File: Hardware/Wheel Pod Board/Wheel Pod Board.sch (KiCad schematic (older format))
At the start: 30 parts, among them U1 STM32F401RCT6

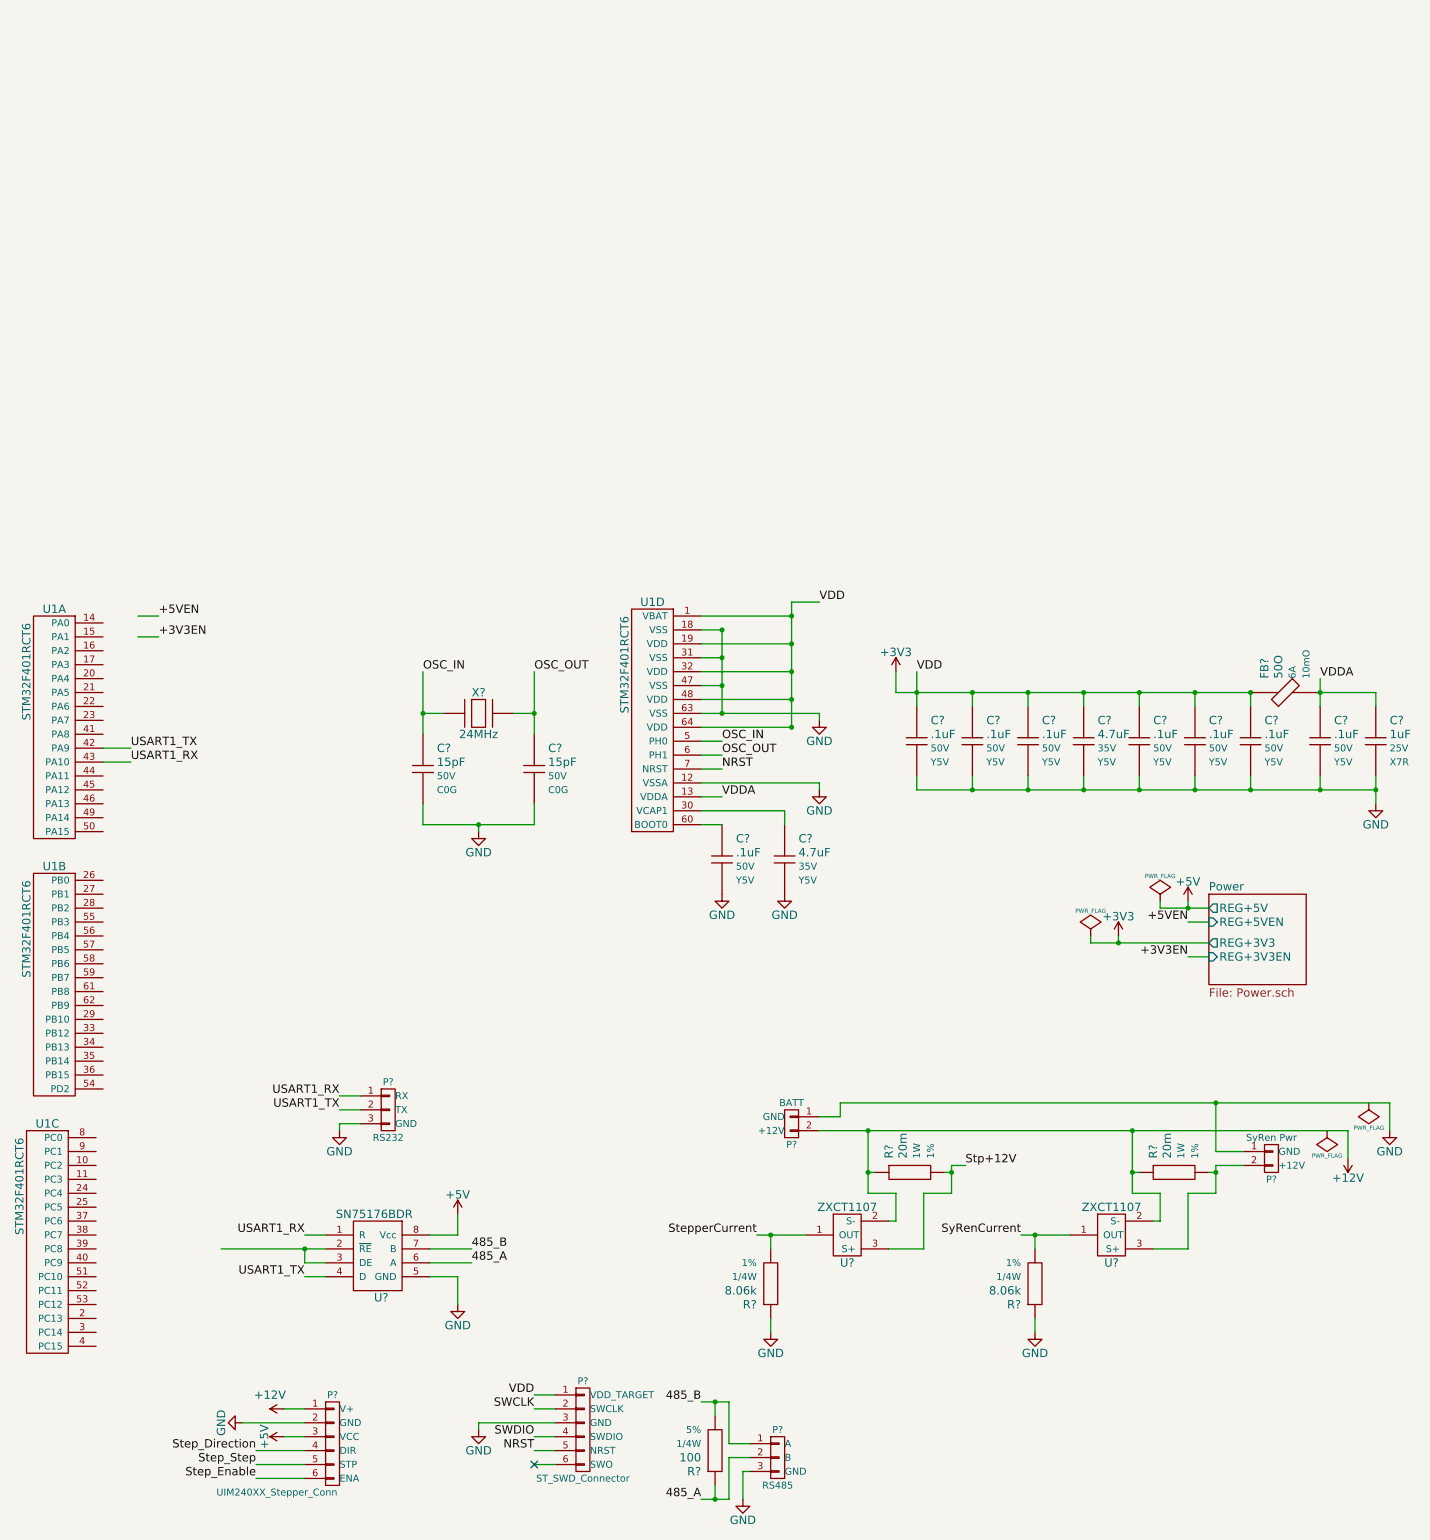
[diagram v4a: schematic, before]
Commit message: Calculate current sense, parts on PCB
Resolves #6
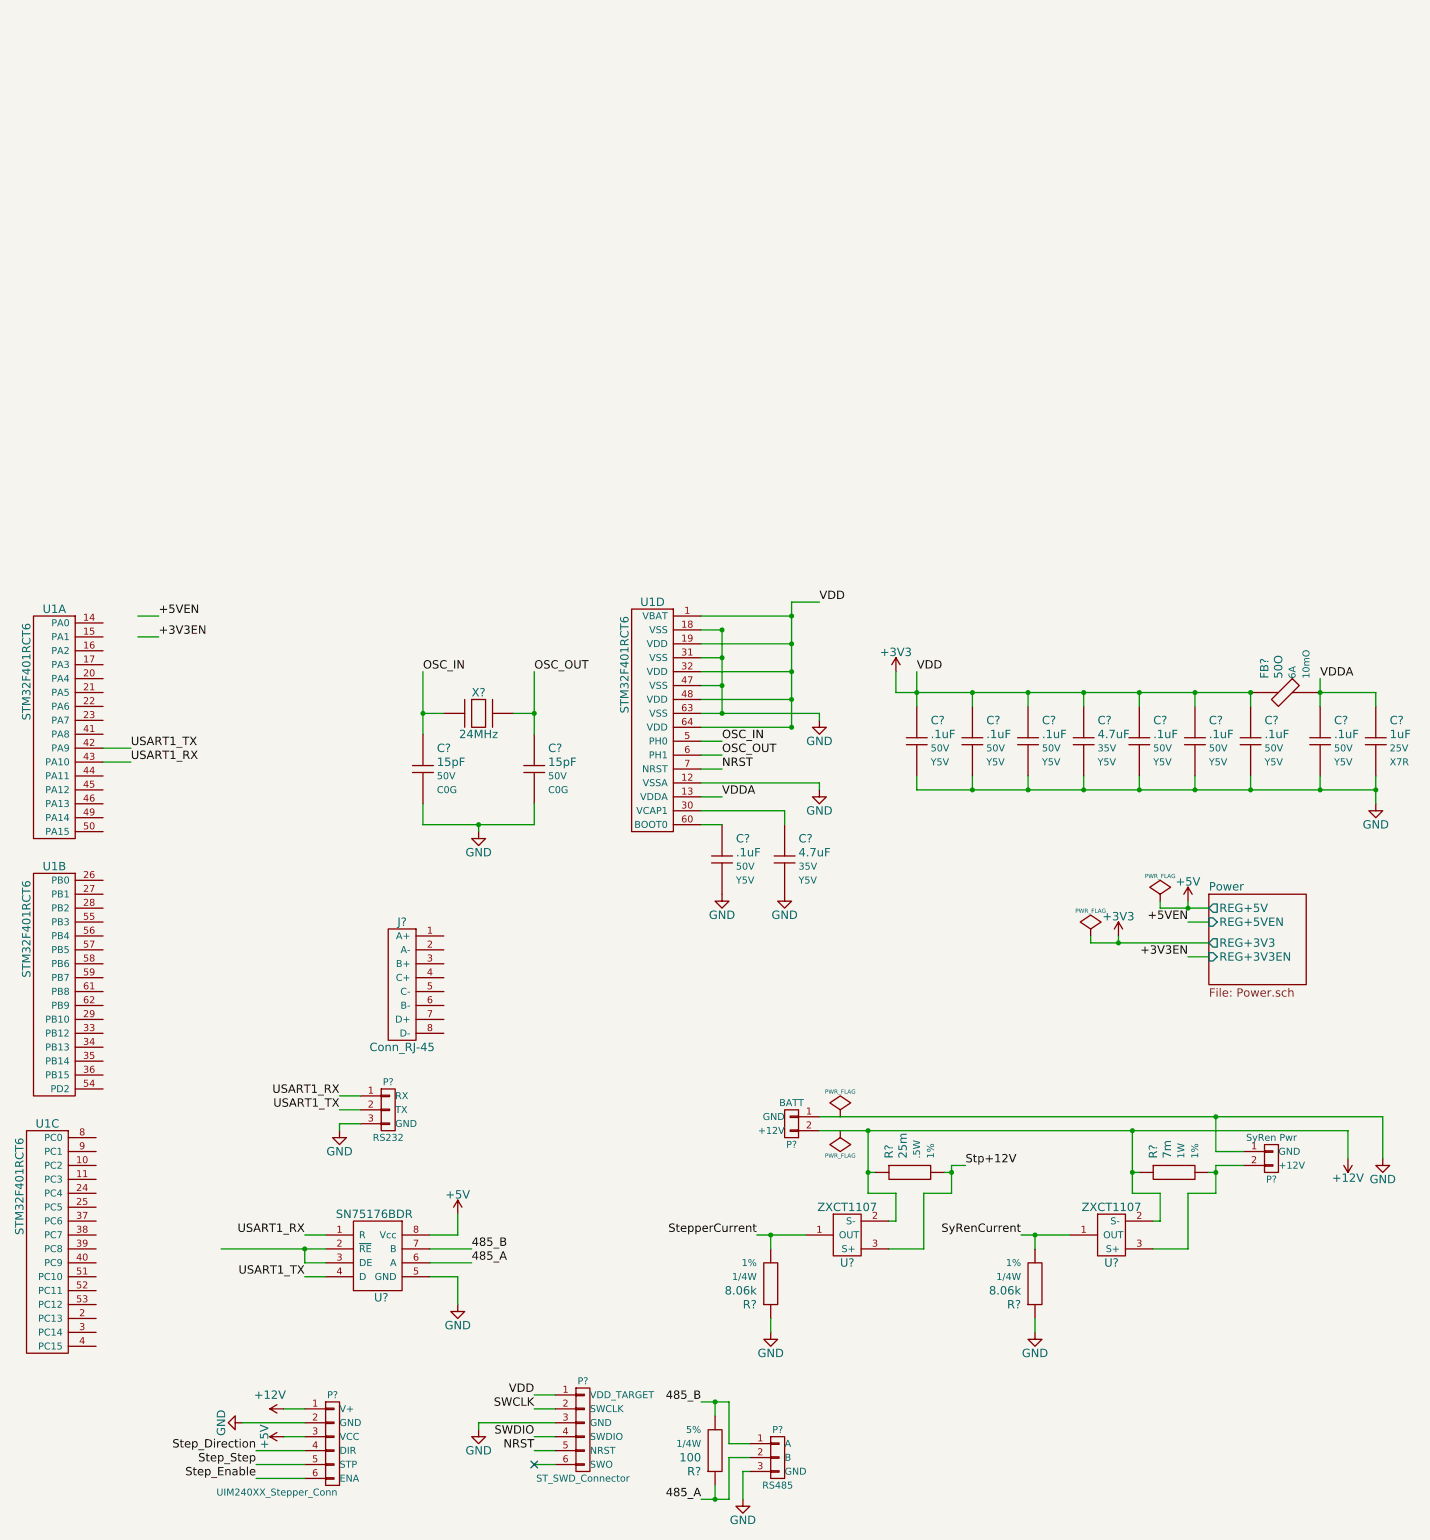
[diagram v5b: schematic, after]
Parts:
- added J?: Conn_RJ-45, symbol Conn_RJ-45
- R?: value 20m -> 25m; Manufacturer Part # LRMAM1206-R02FT5 -> LRC-LRF1206LF-01-R025F; Power 1W -> .5W; Vendor Part # 985-1548-1-ND -> 989-1025-1-ND
- R?: value 20m -> 7m; Manufacturer TT Electronics -> Riedon; Manufacturer Part # LRMAM1206-R02FT5 -> CSR1206-0R007F1; Vendor Part # 985-1548-1-ND -> 696-1373-1-ND
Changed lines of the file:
@@
 LIBS:Passives
 LIBS:MAVRIClib
+LIBS:Connectors
 LIBS:Wheel Pod Board-cache
 EELAYER 25 0
@@
 Connection ~ 6100 1400
 Wire Wire Line
-	5950 1800 6800 1800
+	5950 1800 6100 1800
+Wire Wire Line
+	6100 1800 6800 1800
 Connection ~ 6100 1800
 Wire Wire Line
@@
 Connection ~ 6600 1100
 Wire Wire Line
-	6100 1200 6100 1800
-Wire Wire Line
-	6600 1000 6600 1900
+	6100 1200 6100 1400
+Wire Wire Line
+	6100 1400 6100 1600
+Wire Wire Line
+	6100 1600 6100 1800
+Wire Wire Line
+	6600 1000 6600 1100
+Wire Wire Line
+	6600 1100 6600 1300
+Wire Wire Line
+	6600 1300 6600 1500
+Wire Wire Line
+	6600 1500 6600 1700
+Wire Wire Line
+	6600 1700 6600 1900
 Wire Wire Line
 	5950 2600 6100 2600
@@
 	3100 5750 3250 5750
 Wire Wire Line
-	2500 5650 3250 5650
+	2500 5650 3100 5650
+Wire Wire Line
+	3100 5650 3250 5650
 Wire Wire Line
 	3250 5850 3100 5850
@@
 	9900 1650 9900 1750
 Wire Wire Line
-	7500 1500 7500 1750
+	7500 1500 7500 1650
+Wire Wire Line
+	7500 1650 7500 1750
 Connection ~ 7500 1650
 Wire Wire Line
@@
 Connection ~ 9900 2350
 Wire Wire Line
-	10400 1550 10400 1750
+	10400 1550 10400 1650
+Wire Wire Line
+	10400 1650 10400 1750
 Connection ~ 9900 1650
 Connection ~ 10400 1650
@@
 	10800 1650 10800 1750
 Wire Wire Line
-	10800 2250 10800 2450
+	10800 2250 10800 2350
+Wire Wire Line
+	10800 2350 10800 2450
 Wire Wire Line
 	10400 2350 10400 2250
@@
 	10400 1650 10800 1650
 Wire Wire Line
-	7500 2350 10800 2350
-Wire Wire Line
-	7350 1650 9900 1650
+	7500 2350 7900 2350
+Wire Wire Line
+	7900 2350 8300 2350
+Wire Wire Line
+	8300 2350 8700 2350
+Wire Wire Line
+	8700 2350 9100 2350
+Wire Wire Line
+	9100 2350 9500 2350
+Wire Wire Line
+	9500 2350 9900 2350
+Wire Wire Line
+	9900 2350 10400 2350
+Wire Wire Line
+	10400 2350 10800 2350
+Wire Wire Line
+	7350 1650 7500 1650
+Wire Wire Line
+	7500 1650 7900 1650
+Wire Wire Line
+	7900 1650 8300 1650
+Wire Wire Line
+	8300 1650 8700 1650
+Wire Wire Line
+	8700 1650 9100 1650
+Wire Wire Line
+	9100 1650 9500 1650
+Wire Wire Line
+	9500 1650 9900 1650
 Wire Wire Line
 	7350 1500 7350 1650
@@
 	6150 7150 6150 7450
 Wire Wire Line
-	6150 7450 5950 7450
-Wire Wire Line
-	5950 6750 6150 6750
+	6150 7450 6050 7450
+Wire Wire Line
+	6050 7450 5950 7450
+Wire Wire Line
+	5950 6750 6050 6750
+Wire Wire Line
+	6050 6750 6150 6750
 Wire Wire Line
 	6150 6750 6150 7050
@@
 OSC_OUT
 Wire Wire Line
-	3950 1500 3950 1950
+	3950 1500 3950 1800
+Wire Wire Line
+	3950 1800 3950 1950
 Wire Wire Line
 	3950 1800 4100 1800
@@
 	4600 1800 4750 1800
 Wire Wire Line
-	4750 1500 4750 1950
+	4750 1500 4750 1800
+Wire Wire Line
+	4750 1800 4750 1950
 Wire Wire Line
 	3950 2450 3950 2600
 Wire Wire Line
-	3950 2600 4750 2600
+	3950 2600 4350 2600
+Wire Wire Line
+	4350 2600 4750 2600
 Wire Wire Line
 	4750 2600 4750 2450
@@
 P 7450 5100
 F 0 "R?" V 7300 5200 60  0000 L CNN
-F 1 "20m" V 7400 5200 60  0000 L CNN
+F 1 "25m" V 7400 5200 60  0000 L CNN
 F 2 "Resistors_SMD:R_1206_HandSoldering" H 7350 5100 60  0001 C CNN
 F 3 "" H 7450 5200 60  0001 C CNN
 F 4 "TT Electronics" H 7450 5100 60  0001 C CNN "Manufacturer"
-F 5 "LRMAM1206-R02FT5" H 7450 5100 60  0001 C CNN "Manufacturer Part #"
+F 5 "LRC-LRF1206LF-01-R025F" H 7450 5100 60  0001 C CNN "Manufacturer Part #"
 F 6 "Digi-Key" H 7450 5100 60  0001 C CNN "Vendor"
-F 7 "985-1548-1-ND" H 7450 5100 60  0001 C CNN "Vendor Part #"
-F 8 "1W" V 7500 5200 50  0000 L CNN "Power"
+F 7 "989-1025-1-ND" H 7450 5100 60  0001 C CNN "Vendor Part #"
+F 8 ".5W" V 7500 5200 50  0000 L CNN "Power"
 F 9 "1%" V 7600 5200 50  0000 L CNN "Tolerance"
 	1    7450 5100
@@
 	7350 5250 7350 5450
 Wire Wire Line
-	6350 5550 6700 5550
+	6350 5550 6450 5550
+Wire Wire Line
+	6450 5550 6700 5550
 Wire Wire Line
 	6450 5650 6450 5550
@@
 	7750 5100 7700 5100
 Wire Wire Line
-	7150 4800 7150 5250
+	7150 4800 7150 5100
+Wire Wire Line
+	7150 5100 7150 5250
 Wire Wire Line
 	7200 5100 7150 5100
@@
 $EndComp
 Wire Wire Line
-	8750 3450 9600 3450
+	8750 3450 8950 3450
+Wire Wire Line
+	8950 3450 9600 3450
 Wire Wire Line
 	8950 3450 8950 3400
@@
 $EndComp
 Wire Wire Line
-	9250 3200 9600 3200
+	9250 3200 9450 3200
+Wire Wire Line
+	9450 3200 9600 3200
 Wire Wire Line
 	9250 3200 9250 3150
@@
 $EndComp
 Wire Wire Line
-	7750 5050 7750 5250
+	7750 5050 7750 5100
+Wire Wire Line
+	7750 5100 7750 5250
 Wire Wire Line
 	6450 6150 6450 6250
@@
 StepperCurrent
 Wire Wire Line
-	6800 4800 10600 4800
+	6800 4800 7150 4800
+Wire Wire Line
+	7150 4800 9050 4800
+Wire Wire Line
+	9050 4800 10600 4800
 $Comp
 L ZXCT1107 U?
@@
 P 9350 5100
 F 0 "R?" V 9200 5200 60  0000 L CNN
-F 1 "20m" V 9300 5200 60  0000 L CNN
+F 1 "7m" V 9300 5200 60  0000 L CNN
 F 2 "Resistors_SMD:R_1206_HandSoldering" H 9250 5100 60  0001 C CNN
 F 3 "" H 9350 5200 60  0001 C CNN
-F 4 "TT Electronics" H 9350 5100 60  0001 C CNN "Manufacturer"
-F 5 "LRMAM1206-R02FT5" H 9350 5100 60  0001 C CNN "Manufacturer Part #"
+F 4 "Riedon" H 9350 5100 60  0001 C CNN "Manufacturer"
+F 5 "CSR1206-0R007F1" H 9350 5100 60  0001 C CNN "Manufacturer Part #"
 F 6 "Digi-Key" H 9350 5100 60  0001 C CNN "Vendor"
-F 7 "985-1548-1-ND" H 9350 5100 60  0001 C CNN "Vendor Part #"
+F 7 "696-1373-1-ND" H 9350 5100 60  0001 C CNN "Vendor Part #"
 F 8 "1W" V 9400 5200 50  0000 L CNN "Power"
 F 9 "1%" V 9500 5200 50  0000 L CNN "Tolerance"
@@
 	9250 5250 9250 5450
 Wire Wire Line
-	8250 5550 8600 5550
+	8250 5550 8350 5550
+Wire Wire Line
+	8350 5550 8600 5550
 Wire Wire Line
 	8350 5650 8350 5550
@@
 	9650 5100 9600 5100
 Wire Wire Line
-	9050 4800 9050 5250
+	9050 4800 9050 5100
+Wire Wire Line
+	9050 5100 9050 5250
 Wire Wire Line
 	9100 5100 9050 5100
@@
 	6800 4700 6950 4700
 Wire Wire Line
-	6950 4700 6950 4600
-Wire Wire Line
-	6950 4600 10900 4600
-Wire Wire Line
-	10900 4600 10900 4800
+	6950 4700 6950 4700
+Wire Wire Line
+	6950 4700 9650 4700
+Wire Wire Line
+	9650 4700 10850 4700
+Wire Wire Line
+	10850 4700 10850 5000
 $Comp
 L GND #PWR?
 U 1 1 54F987F3
-P 10900 4800
-F 0 "#PWR?" H 10900 4550 60  0001 C CNN
-F 1 "GND" H 10900 4650 60  0000 C CNN
-F 2 "" H 10900 4800 60  0000 C CNN
-F 3 "" H 10900 4800 60  0000 C CNN
-	1    10900 4800
+P 10850 5000
+F 0 "#PWR?" H 10850 4750 60  0001 C CNN
+F 1 "GND" H 10850 4850 60  0000 C CNN
+F 2 "" H 10850 5000 60  0000 C CNN
+F 3 "" H 10850 5000 60  0000 C CNN
+	1    10850 5000
 	1    0    0    -1
 $EndComp
@@
 Connection ~ 7150 4800
 Wire Wire Line
-	9650 5050 9650 5250
+	9650 5050 9650 5100
+Wire Wire Line
+	9650 5100 9650 5250
 Wire Wire Line
 	9650 5050 9850 5050
@@
 L PWR_FLAG #FLG?
 U 1 1 54F9E134
-P 10450 4800
-F 0 "#FLG?" H 10450 4895 30  0001 C CNN
-F 1 "PWR_FLAG" H 10450 4980 30  0000 C CNN
-F 2 "" H 10450 4800 60  0000 C CNN
-F 3 "" H 10450 4800 60  0000 C CNN
-	1    10450 4800
+P 6950 4800
+F 0 "#FLG?" H 6950 4895 30  0001 C CNN
+F 1 "PWR_FLAG" H 6950 4980 30  0000 C CNN
+F 2 "" H 6950 4800 60  0000 C CNN
+F 3 "" H 6950 4800 60  0000 C CNN
+	1    6950 4800
 	-1   0    0    1
 $EndComp
@@
 L PWR_FLAG #FLG?
 U 1 1 54F9E417
-P 10750 4600
-F 0 "#FLG?" H 10750 4695 30  0001 C CNN
-F 1 "PWR_FLAG" H 10750 4780 30  0000 C CNN
-F 2 "" H 10750 4600 60  0000 C CNN
-F 3 "" H 10750 4600 60  0000 C CNN
-	1    10750 4600
-	-1   0    0    1
+P 6950 4700
+F 0 "#FLG?" H 6950 4795 30  0001 C CNN
+F 1 "PWR_FLAG" H 6950 4880 30  0000 C CNN
+F 2 "" H 6950 4700 60  0000 C CNN
+F 3 "" H 6950 4700 60  0000 C CNN
+	1    6950 4700
+	1    0    0    -1
 $EndComp
 Wire Wire Line
 	9850 4950 9650 4950
 Wire Wire Line
-	9650 4950 9650 4600
-Connection ~ 9650 4600
+	9650 4950 9650 4700
+Connection ~ 9650 4700
 $Comp
 L +3V3 #PWR?
@@
 Wire Wire Line
 	3350 4550 3500 4550
+$Comp
+L Conn_RJ-45 J?
+U 1 1 54FA3CB5
+P 3800 3750
+F 0 "J?" H 3800 4200 60  0000 C CNN
+F 1 "Conn_RJ-45" H 3800 3300 60  0000 C CNN
+F 2 "" H 3800 4050 60  0000 C CNN
+F 3 "" H 3800 4050 60  0000 C CNN
+	1    3800 3750
+	1    0    0    -1
+$EndComp
 $EndSCHEMATC

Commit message: More parts on PCB
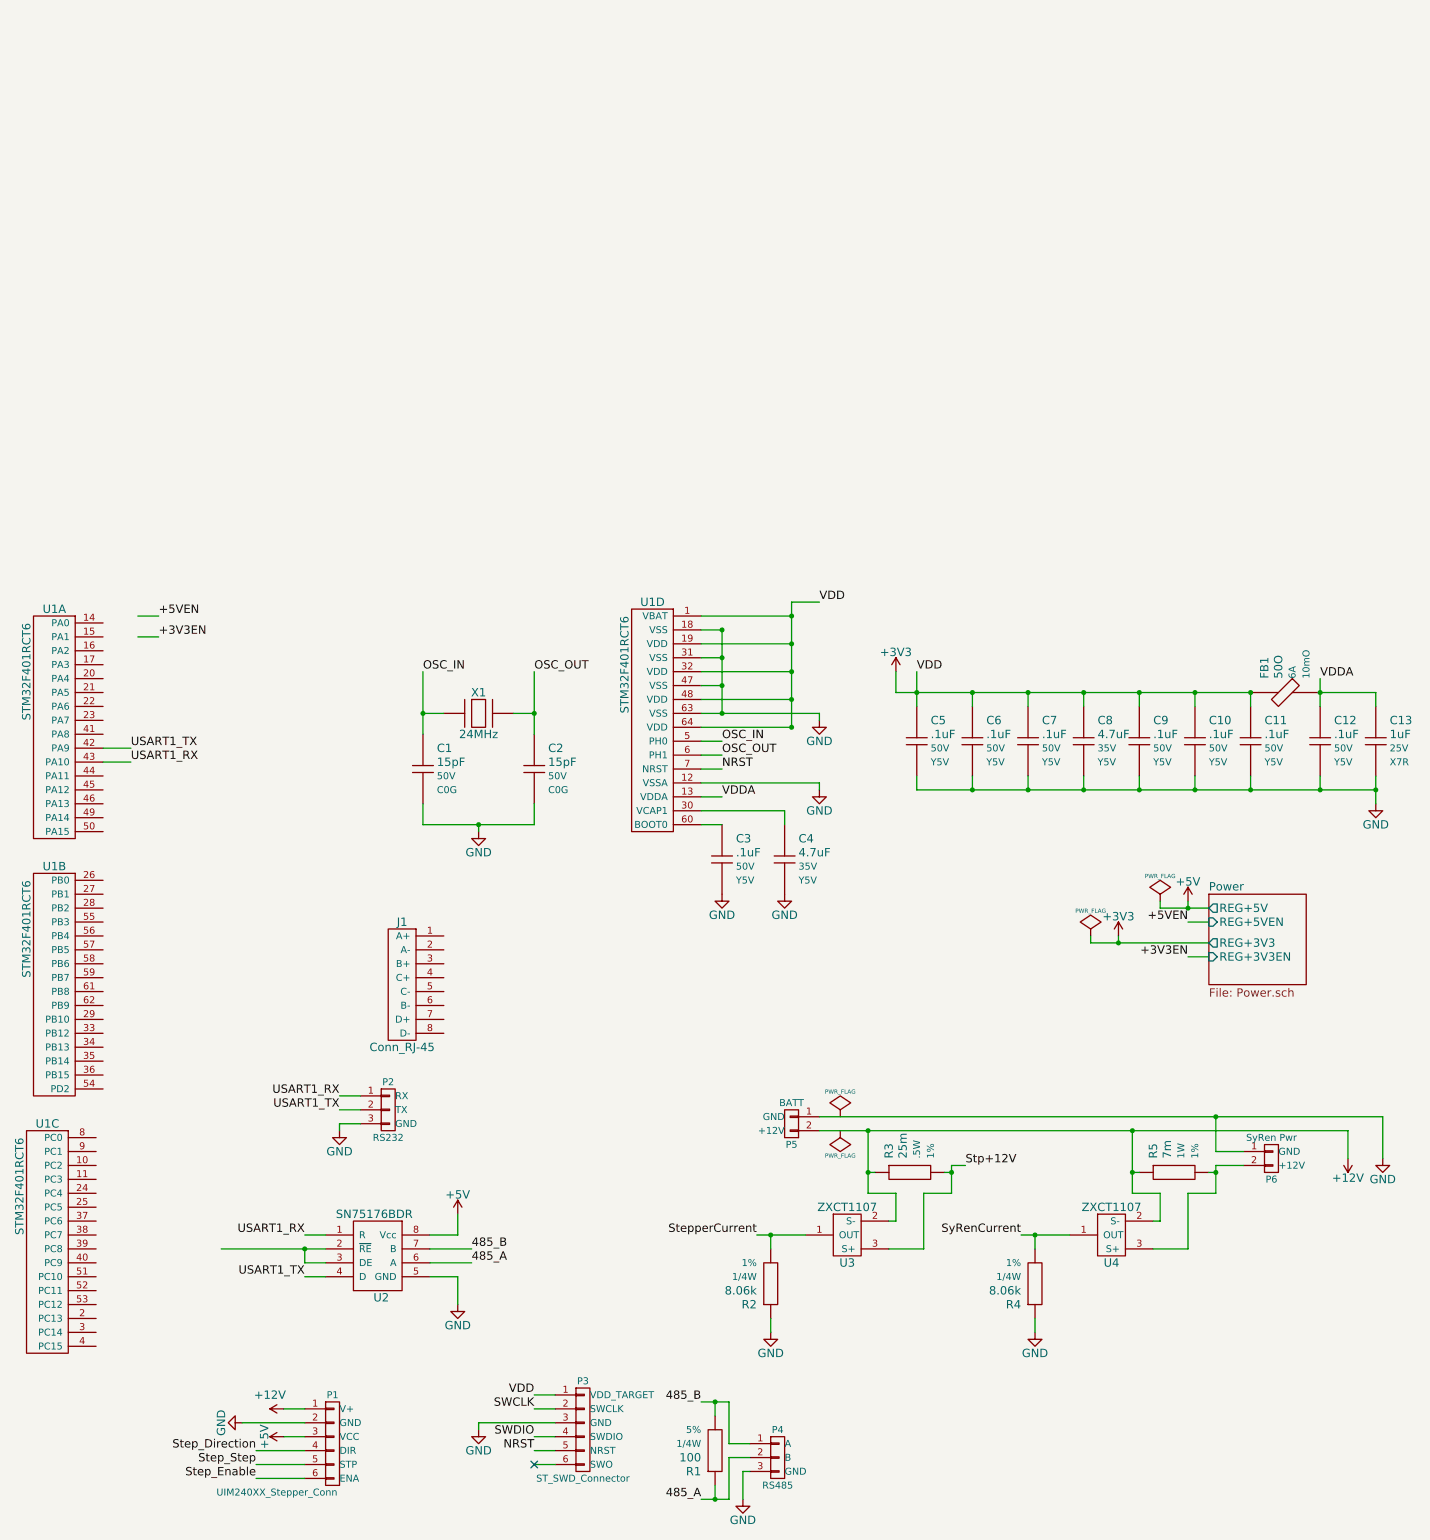
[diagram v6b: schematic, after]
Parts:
- J1: renamed from J?; footprint (none) -> Connect:RJ45_8
- P2: renamed from P?; footprint (none) -> MAVRIC_footprints:1x3_SMD_header
- P5, P6: renamed from P?; footprint (none) -> MAVRIC_footprints:1x2_SMD_header
- U3, U4: renamed from U?; footprint Housings_SOT-23_SOT-143_TSOT-6:SOT23_Transistor_Handsoldering_RevB_14Mar2014 -> Housings_SOT-23_SOT-143_TSOT-6:SOT23_Handsoldering
- gave numbers to parts that had none: 24
